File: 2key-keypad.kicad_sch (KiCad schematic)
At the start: 14 parts, among them SW1 SW_Push, U1 ATmega32U4-A, Y1 16MHz

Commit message: Updated schematic
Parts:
- added D1, D2: D_Small, Diode_SMD:D_SOD-123, symbol Device:D_Small
- added F1: 500mA, Fuse:Fuse_1206_3216Metric, symbol Device:Polyfuse
- added MX1, MX2: MX-NoLED, MX_Alps_Hybrid:MX-1U, symbol MX_Alps_Hybrid:MX-NoLED
- added USB1: Molex-0548190589, random-keyboard-parts:Molex-0548190589, symbol random-keyboard-parts:Molex-0548190589
- C1, C2, C3, C4, C6, C7: footprint (none) -> Capacitor_SMD:C_0805_2012Metric
- C5: value 0.1uF -> 10uF; footprint (none) -> Capacitor_SMD:C_0805_2012Metric
- R1, R2, R3, R4: footprint (none) -> Resistor_SMD:R_0805_2012Metric
- SW1: footprint (none) -> random-keyboard-parts:SKQG-1155865
- Y1: footprint (none) -> Crystal:Crystal_SMD_3225-4Pin_3.2x2.5mm
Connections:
- net +5V: now also F1.2
- net D+: now also USB1.3 (D+)
- net D-: now also USB1.4 (D-)
- net GND: now also USB1.1 (GND)
- net ROW0: now reaches U1.27 (PD7)
- net ROW0: now also D1.1 (K), D2.1 (K)
- net COL1: now reaches U1.28 (PB4)
- net COL1: now also MX2.1 (COL)
- net COL0: now reaches U1.29 (PB5)
- net COL0: now also MX1.1 (COL)
- new net: D2.2 (A), MX2.2 (ROW)
- new net: D1.2 (A), MX1.2 (ROW)
- new net VCC: F1.1, USB1.5 (VBUS)
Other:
- note removed: "PCB Guide Part 4 step 6"

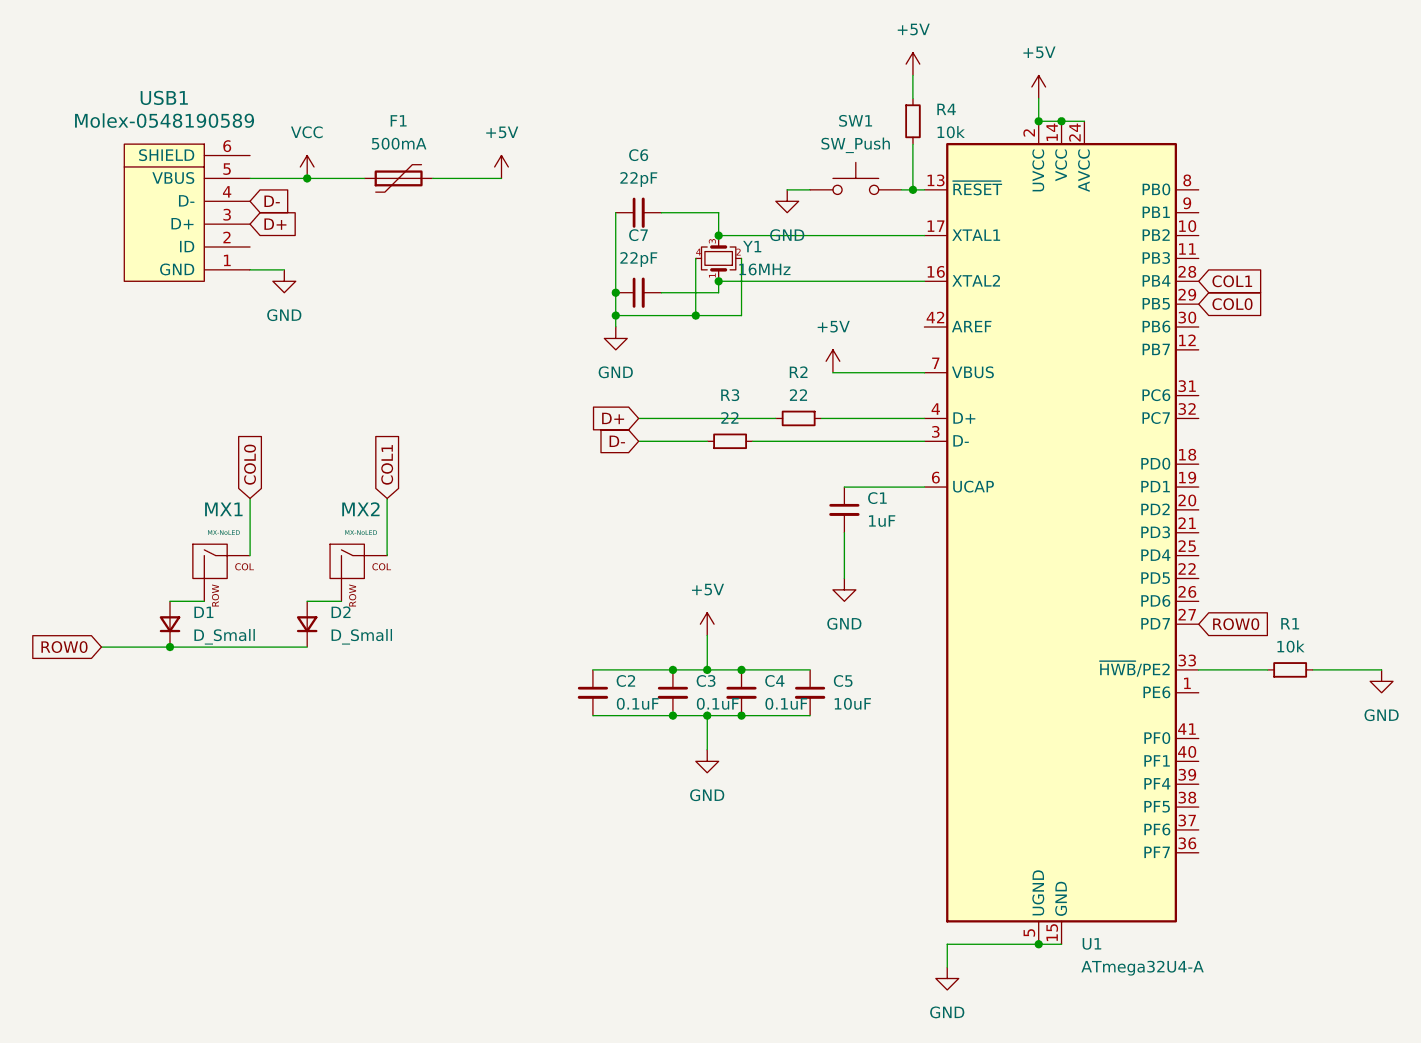
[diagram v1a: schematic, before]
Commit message: Routed PCB - missing key matrix
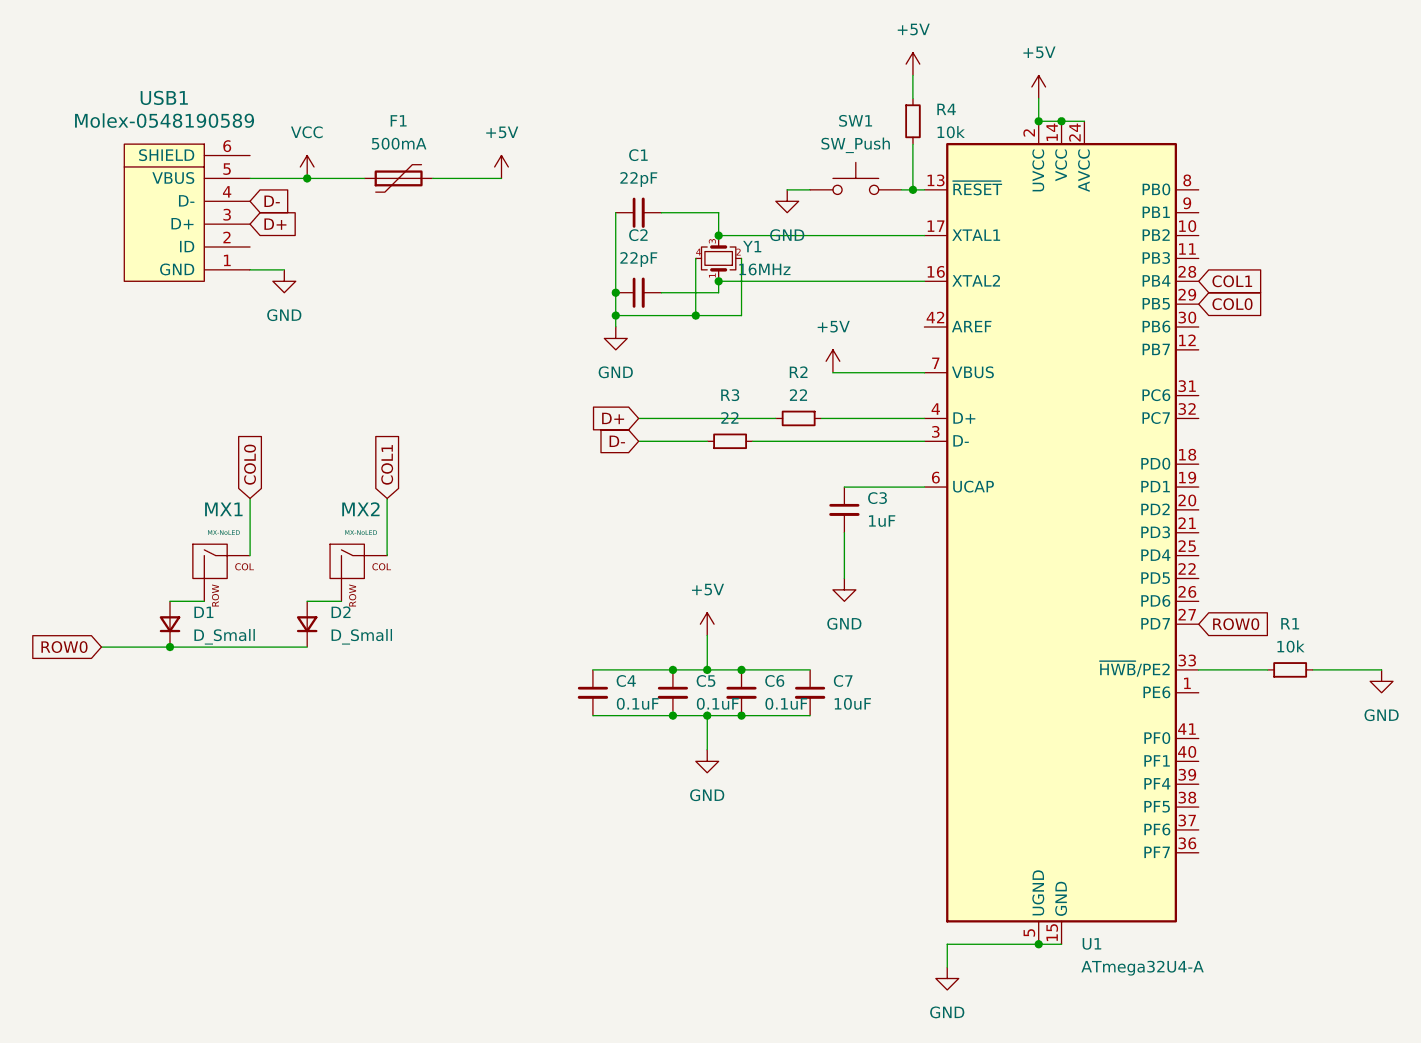
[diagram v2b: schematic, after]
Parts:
- renumbered C6 to C1, C7 to C2, C1 to C3, C2 to C4, C3 to C5, C4 to C6, C5 to C7
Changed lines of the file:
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@@
   (symbol (lib_id "Device:C_Small") (at 176.53 31.75 90) (unit 1)
     (in_bom yes) (on_board yes) (dnp no) (fields_autoplaced)
-    (property "Reference" "C6" (at 176.5363 25.4 90)
+    (property "Reference" "C1" (at 176.5363 25.4 90)
       (effects (font (size 1.27 1.27)))
     )
@@
       (project "2key-keypad"
         (path "/2ca9f8c5-0c03-4250-b620-ee8da924d452"
-          (reference "C6") (unit 1)
+          (reference "C1") (unit 1)
         )
       )
@@
   (symbol (lib_id "Device:C_Small") (at 176.53 40.64 90) (unit 1)
     (in_bom yes) (on_board yes) (dnp no) (fields_autoplaced)
-    (property "Reference" "C7" (at 176.5363 34.29 90)
+    (property "Reference" "C2" (at 176.5363 34.29 90)
       (effects (font (size 1.27 1.27)))
     )
@@
       (project "2key-keypad"
         (path "/2ca9f8c5-0c03-4250-b620-ee8da924d452"
-          (reference "C7") (unit 1)
+          (reference "C2") (unit 1)
         )
       )
@@
   (symbol (lib_id "Device:C_Small") (at 171.45 85.09 0) (unit 1)
     (in_bom yes) (on_board yes) (dnp no) (fields_autoplaced)
-    (property "Reference" "C2" (at 173.99 83.8263 0)
+    (property "Reference" "C4" (at 173.99 83.8263 0)
       (effects (font (size 1.27 1.27)) (justify left))
     )
@@
       (project "2key-keypad"
         (path "/2ca9f8c5-0c03-4250-b620-ee8da924d452"
-          (reference "C2") (unit 1)
+          (reference "C4") (unit 1)
         )
       )
@@
   (symbol (lib_id "Device:C_Small") (at 180.34 85.09 0) (unit 1)
     (in_bom yes) (on_board yes) (dnp no) (fields_autoplaced)
-    (property "Reference" "C3" (at 182.88 83.8263 0)
+    (property "Reference" "C5" (at 182.88 83.8263 0)
       (effects (font (size 1.27 1.27)) (justify left))
     )
@@
       (project "2key-keypad"
         (path "/2ca9f8c5-0c03-4250-b620-ee8da924d452"
-          (reference "C3") (unit 1)
+          (reference "C5") (unit 1)
         )
       )
@@
   (symbol (lib_id "Device:C_Small") (at 199.39 64.77 0) (unit 1)
     (in_bom yes) (on_board yes) (dnp no) (fields_autoplaced)
-    (property "Reference" "C1" (at 201.93 63.5063 0)
+    (property "Reference" "C3" (at 201.93 63.5063 0)
       (effects (font (size 1.27 1.27)) (justify left))
     )
@@
       (project "2key-keypad"
         (path "/2ca9f8c5-0c03-4250-b620-ee8da924d452"
-          (reference "C1") (unit 1)
+          (reference "C3") (unit 1)
         )
       )
@@
   (symbol (lib_id "Device:C_Small") (at 187.96 85.09 0) (unit 1)
     (in_bom yes) (on_board yes) (dnp no) (fields_autoplaced)
-    (property "Reference" "C4" (at 190.5 83.8263 0)
+    (property "Reference" "C6" (at 190.5 83.8263 0)
       (effects (font (size 1.27 1.27)) (justify left))
     )
@@
       (project "2key-keypad"
         (path "/2ca9f8c5-0c03-4250-b620-ee8da924d452"
-          (reference "C4") (unit 1)
+          (reference "C6") (unit 1)
         )
       )
@@
   (symbol (lib_id "Device:C_Small") (at 195.58 85.09 0) (unit 1)
     (in_bom yes) (on_board yes) (dnp no) (fields_autoplaced)
-    (property "Reference" "C5" (at 198.12 83.8263 0)
+    (property "Reference" "C7" (at 198.12 83.8263 0)
       (effects (font (size 1.27 1.27)) (justify left))
     )
@@
       (project "2key-keypad"
         (path "/2ca9f8c5-0c03-4250-b620-ee8da924d452"
-          (reference "C5") (unit 1)
-        )
-      )
+          (reference "C7") (unit 1)
+        )
+      )

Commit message: Finished First Schem
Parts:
- MX1, MX2: footprint MX_Alps_Hybrid:MX-1U -> MX_Only:MXOnly-1U-Hotswap
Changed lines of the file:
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@@
       (effects (font (size 0.508 0.508)))
     )
-    (property "Footprint" "MX_Alps_Hybrid:MX-1U" (at 113.665 71.755 0)
+    (property "Footprint" "MX_Only:MXOnly-1U-Hotswap" (at 113.665 71.755 0)
       (effects (font (size 1.524 1.524)) hide)
     )
@@
       (effects (font (size 0.508 0.508)))
     )
-    (property "Footprint" "MX_Alps_Hybrid:MX-1U" (at 128.905 71.755 0)
+    (property "Footprint" "MX_Only:MXOnly-1U-Hotswap" (at 128.905 71.755 0)
       (effects (font (size 1.524 1.524)) hide)
     )
